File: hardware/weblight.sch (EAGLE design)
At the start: 14 parts, among them U1 ATtiny85-20SU

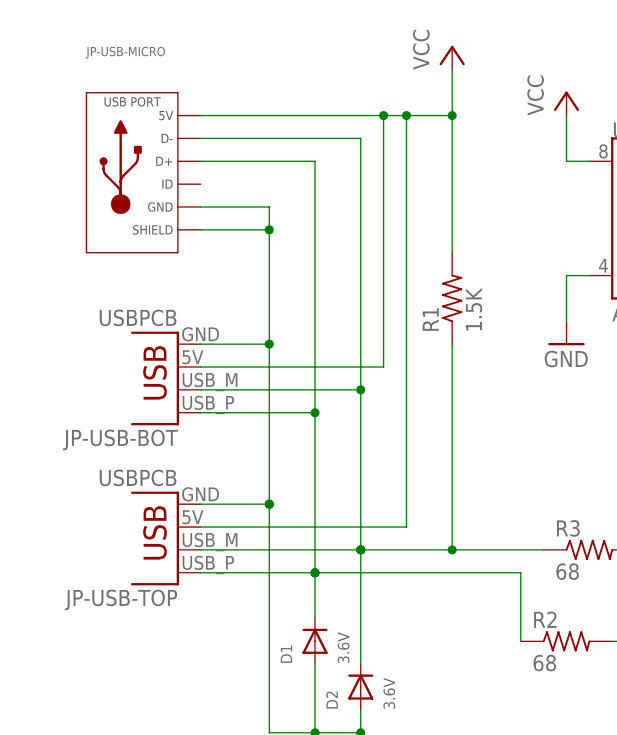
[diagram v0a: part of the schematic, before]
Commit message: #2: Remove bottom USB connector to avoid short
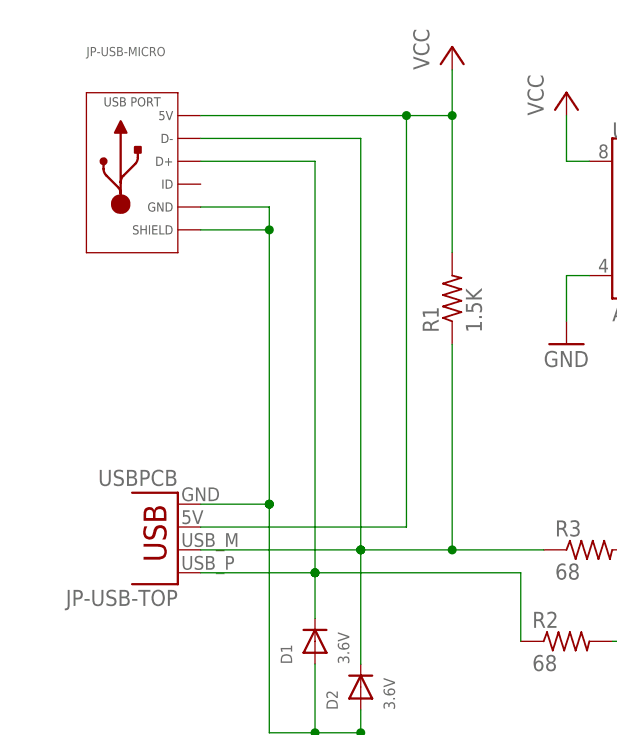
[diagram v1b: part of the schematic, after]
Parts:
- removed JP-USB-BOT: USBPCB, SparkFun-Connectors:USBPCB
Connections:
- net GND: no longer JP-USB-BOT.GND
- net USB_D_MINUS_RAW: no longer JP-USB-BOT.D-
- net USB_D_PLUS_RAW: no longer JP-USB-BOT.D+
- net VCC: no longer JP-USB-BOT.VBUS
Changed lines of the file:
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@@
 <part name="D2" library="microbuilder" deviceset="DIODE" device="SOD-523" value="3.6V"/>
 <part name="D4" library="SparkFun-LED" deviceset="WS2812B" device="" value="WS2812B"/>
-<part name="JP-USB-BOT" library="SparkFun-Connectors" deviceset="USB" device="PCB"/>
 <part name="U1" library="SparkFun-DigitalIC" deviceset="ATTINY45" device="TINY85-20-SMT" value="ATtiny85-20SU"/>
 <part name="JP-USB-MICRO" library="MF_Connectors" deviceset="USB" device="_MICRO_RIGHT"/>
@@
 <instance part="D2" gate="G$1" x="-27.94" y="22.86" rot="R90"/>
 <instance part="D4" gate="G$1" x="73.66" y="45.72"/>
-<instance part="JP-USB-BOT" gate="G$1" x="-48.26" y="60.96" rot="R180"/>
 <instance part="U1" gate="G$1" x="12.7" y="73.66"/>
 <instance part="JP-USB-MICRO" gate="G$1" x="-53.34" y="81.28"/>
@@
 <wire x1="-45.72" y1="40.64" x2="-22.86" y2="40.64" width="0.1524" layer="91"/>
 <pinref part="R1" gate="G$1" pin="2"/>
-<pinref part="JP-USB-BOT" gate="G$1" pin="VBUS"/>
-<wire x1="-45.72" y1="58.42" x2="-25.4" y2="58.42" width="0.1524" layer="91"/>
 <pinref part="JP-USB-MICRO" gate="G$1" pin="5V"/>
 <wire x1="-17.78" y1="86.36" x2="-22.86" y2="86.36" width="0.1524" layer="91"/>
 <junction x="-17.78" y="86.36"/>
 <pinref part="P+2" gate="VCC" pin="VCC"/>
-<wire x1="-22.86" y1="86.36" x2="-25.4" y2="86.36" width="0.1524" layer="91"/>
-<wire x1="-25.4" y1="86.36" x2="-45.72" y2="86.36" width="0.1524" layer="91"/>
+<wire x1="-22.86" y1="86.36" x2="-45.72" y2="86.36" width="0.1524" layer="91"/>
 <wire x1="-17.78" y1="86.36" x2="-17.78" y2="91.44" width="0.1524" layer="91"/>
 <wire x1="-17.78" y1="71.12" x2="-17.78" y2="86.36" width="0.1524" layer="91"/>
-<wire x1="-25.4" y1="58.42" x2="-25.4" y2="86.36" width="0.1524" layer="91"/>
-<junction x="-25.4" y="86.36"/>
 <wire x1="-22.86" y1="40.64" x2="-22.86" y2="86.36" width="0.1524" layer="91"/>
 <junction x="-22.86" y="86.36"/>
@@
 <pinref part="JP-USB-TOP" gate="G$1" pin="GND"/>
 <wire x1="-45.72" y1="43.18" x2="-38.1" y2="43.18" width="0.1524" layer="91"/>
-<pinref part="JP-USB-BOT" gate="G$1" pin="GND"/>
-<wire x1="-45.72" y1="60.96" x2="-38.1" y2="60.96" width="0.1524" layer="91"/>
 <pinref part="JP-USB-MICRO" gate="G$1" pin="SLD"/>
 <junction x="-38.1" y="73.66"/>
@@
 <wire x1="-45.72" y1="76.2" x2="-38.1" y2="76.2" width="0.1524" layer="91"/>
 <wire x1="-38.1" y1="76.2" x2="-38.1" y2="73.66" width="0.1524" layer="91"/>
-<wire x1="-38.1" y1="73.66" x2="-38.1" y2="60.96" width="0.1524" layer="91"/>
-<junction x="-38.1" y="60.96"/>
-<wire x1="-38.1" y1="60.96" x2="-38.1" y2="43.18" width="0.1524" layer="91"/>
+<wire x1="-38.1" y1="73.66" x2="-38.1" y2="43.18" width="0.1524" layer="91"/>
 <junction x="-38.1" y="43.18"/>
 <junction x="-38.1" y="43.18"/>
@@
 <wire x1="-27.94" y1="25.4" x2="-27.94" y2="38.1" width="0.1524" layer="91"/>
 <junction x="-27.94" y="38.1"/>
-<pinref part="JP-USB-BOT" gate="G$1" pin="D-"/>
-<wire x1="-45.72" y1="55.88" x2="-27.94" y2="55.88" width="0.1524" layer="91"/>
 <junction x="-27.94" y="38.1"/>
-<wire x1="-27.94" y1="55.88" x2="-27.94" y2="38.1" width="0.1524" layer="91"/>
-<junction x="-27.94" y="55.88"/>
-<wire x1="-27.94" y1="55.88" x2="-27.94" y2="83.82" width="0.1524" layer="91"/>
+<wire x1="-27.94" y1="38.1" x2="-27.94" y2="83.82" width="0.1524" layer="91"/>
 <pinref part="JP-USB-MICRO" gate="G$1" pin="D-"/>
 <wire x1="-27.94" y1="83.82" x2="-45.72" y2="83.82" width="0.1524" layer="91"/>
@@
 <wire x1="-33.02" y1="30.48" x2="-33.02" y2="35.56" width="0.1524" layer="91"/>
 <junction x="-33.02" y="35.56"/>
-<pinref part="JP-USB-BOT" gate="G$1" pin="D+"/>
-<wire x1="-45.72" y1="53.34" x2="-33.02" y2="53.34" width="0.1524" layer="91"/>
 <junction x="-33.02" y="35.56"/>
-<wire x1="-33.02" y1="53.34" x2="-33.02" y2="35.56" width="0.1524" layer="91"/>
-<junction x="-33.02" y="53.34"/>
 <pinref part="JP-USB-MICRO" gate="G$1" pin="D+"/>
-<wire x1="-33.02" y1="53.34" x2="-33.02" y2="81.28" width="0.1524" layer="91"/>
+<wire x1="-33.02" y1="35.56" x2="-33.02" y2="81.28" width="0.1524" layer="91"/>
 <wire x1="-33.02" y1="81.28" x2="-45.72" y2="81.28" width="0.1524" layer="91"/>
 </segment>

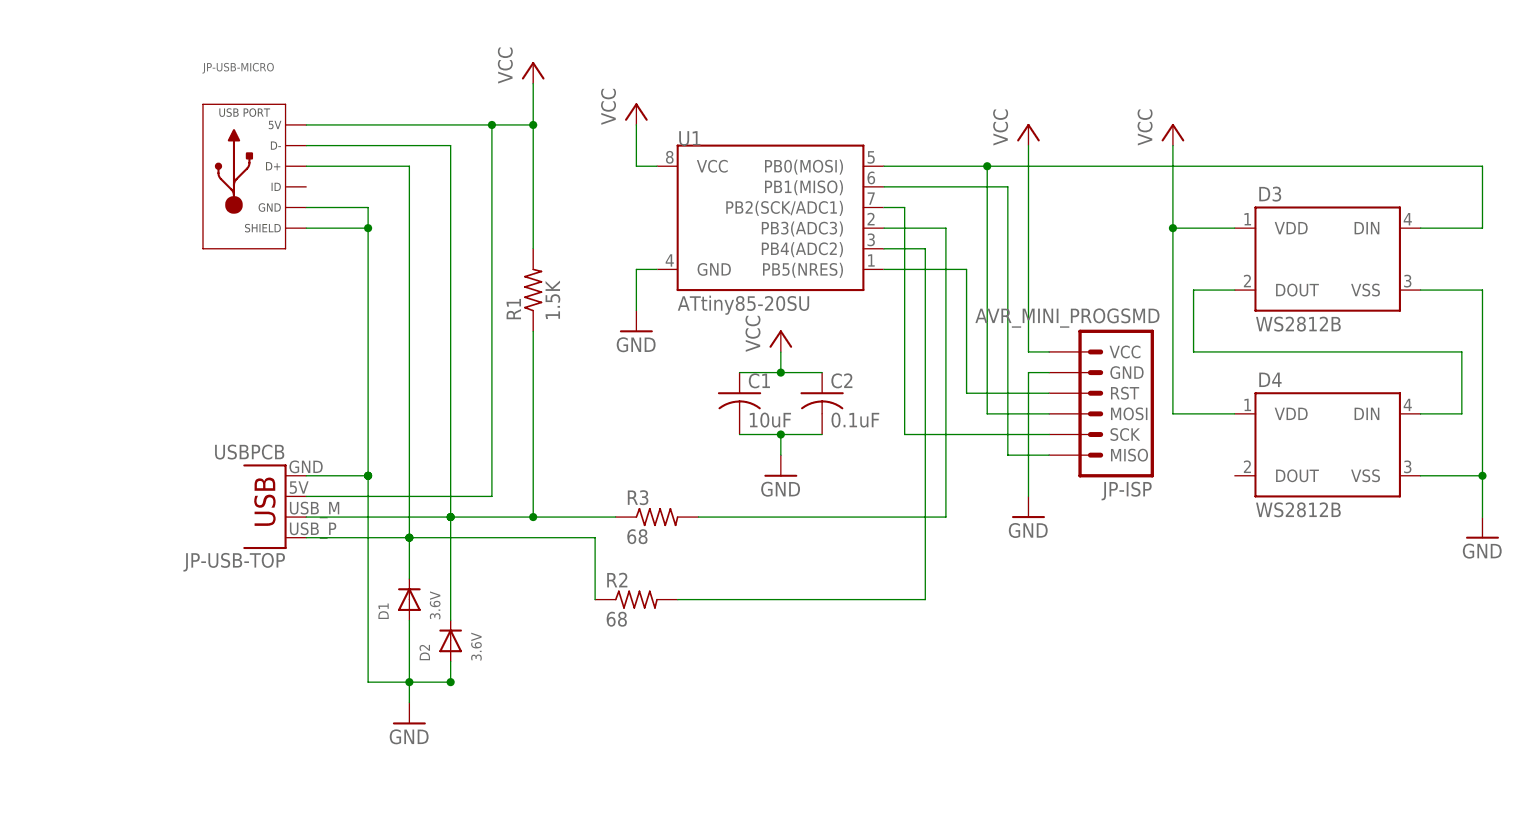
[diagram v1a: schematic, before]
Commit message: #17: add 470 ohm resistor before first DIN
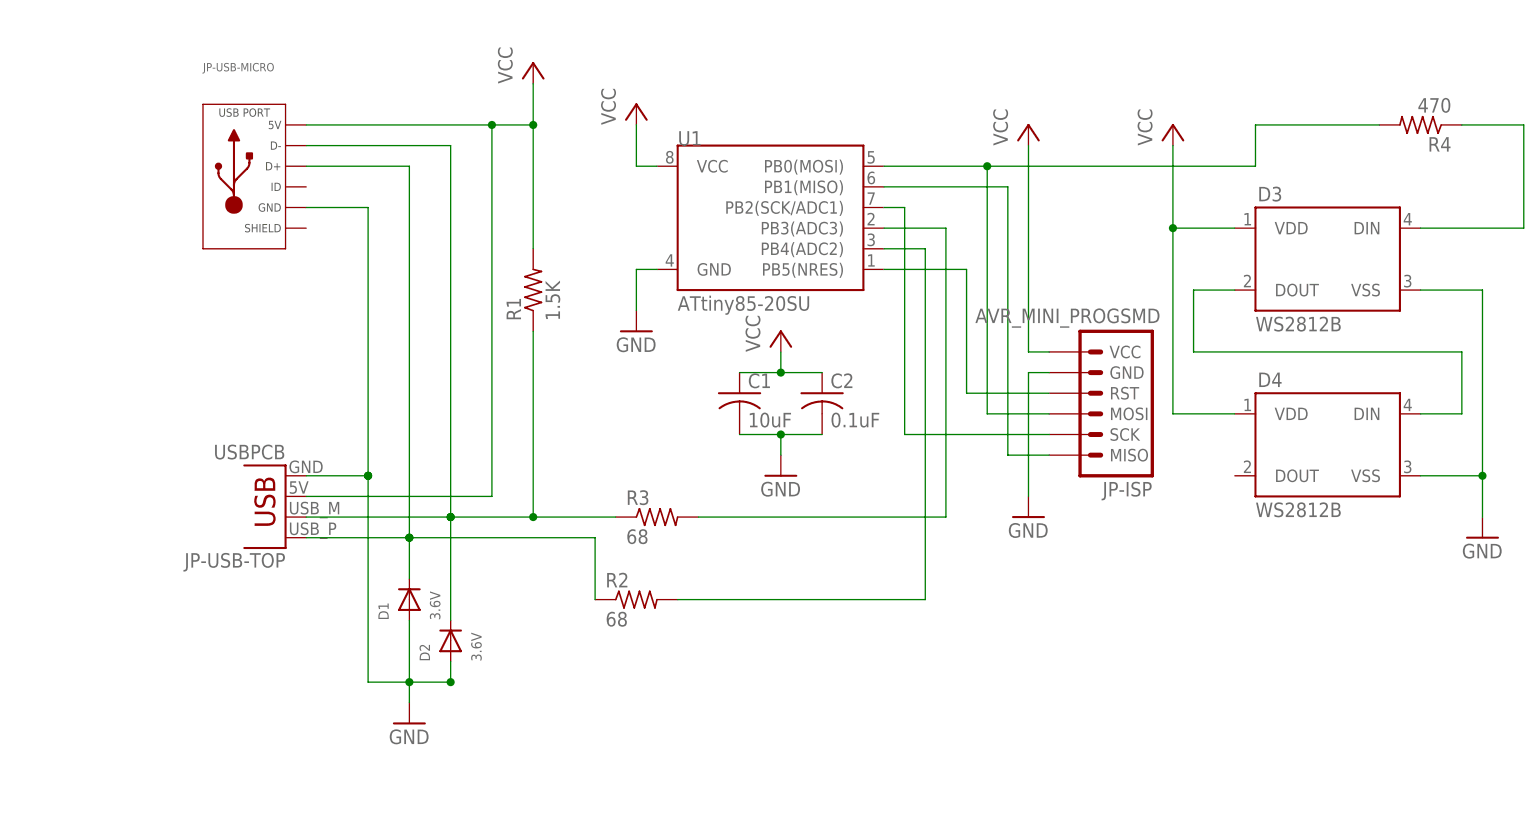
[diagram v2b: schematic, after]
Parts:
- added R4: 470, rcl:R-US_R0402
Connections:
- new net N$1: D3.DIN, R4.1
- net GND: no longer JP-USB-MICRO.SLD
- net MOSI/DIN: now also R4.2; no longer D3.DIN
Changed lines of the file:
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@@
 <grid distance="0.1" unitdist="inch" unit="inch" style="lines" multiple="1" display="no" altdistance="0.01" altunitdist="inch" altunit="inch"/>
 <layers>
-<layer number="1" name="Top" color="4" fill="1" visible="no" active="no"/>
-<layer number="16" name="Bottom" color="1" fill="1" visible="no" active="no"/>
-<layer number="17" name="Pads" color="2" fill="1" visible="no" active="no"/>
-<layer number="18" name="Vias" color="2" fill="1" visible="no" active="no"/>
-<layer number="19" name="Unrouted" color="6" fill="1" visible="no" active="no"/>
-<layer number="20" name="Dimension" color="15" fill="1" visible="no" active="no"/>
-<layer number="21" name="tPlace" color="7" fill="1" visible="no" active="no"/>
-<layer number="22" name="bPlace" color="7" fill="1" visible="no" active="no"/>
-<layer number="23" name="tOrigins" color="15" fill="1" visible="no" active="no"/>
-<layer number="24" name="bOrigins" color="15" fill="1" visible="no" active="no"/>
-<layer number="25" name="tNames" color="7" fill="1" visible="no" active="no"/>
-<layer number="26" name="bNames" color="7" fill="1" visible="no" active="no"/>
-<layer number="27" name="tValues" color="7" fill="1" visible="no" active="no"/>
-<layer number="28" name="bValues" color="7" fill="1" visible="no" active="no"/>
+<layer number="1" name="Top" color="4" fill="1" visible="yes" active="no"/>
+<layer number="16" name="Bottom" color="1" fill="1" visible="yes" active="no"/>
+<layer number="17" name="Pads" color="2" fill="1" visible="yes" active="no"/>
+<layer number="18" name="Vias" color="2" fill="1" visible="yes" active="no"/>
+<layer number="19" name="Unrouted" color="6" fill="1" visible="yes" active="no"/>
+<layer number="20" name="Dimension" color="15" fill="1" visible="yes" active="no"/>
+<layer number="21" name="tPlace" color="7" fill="1" visible="yes" active="no"/>
+<layer number="22" name="bPlace" color="7" fill="1" visible="yes" active="no"/>
+<layer number="23" name="tOrigins" color="15" fill="1" visible="yes" active="no"/>
+<layer number="24" name="bOrigins" color="15" fill="1" visible="yes" active="no"/>
+<layer number="25" name="tNames" color="7" fill="1" visible="yes" active="no"/>
+<layer number="26" name="bNames" color="7" fill="1" visible="yes" active="no"/>
+<layer number="27" name="tValues" color="7" fill="1" visible="yes" active="no"/>
+<layer number="28" name="bValues" color="7" fill="1" visible="yes" active="no"/>
 <layer number="29" name="tStop" color="7" fill="3" visible="no" active="no"/>
 <layer number="30" name="bStop" color="7" fill="6" visible="no" active="no"/>
@@
 <layer number="35" name="tGlue" color="7" fill="4" visible="no" active="no"/>
 <layer number="36" name="bGlue" color="7" fill="5" visible="no" active="no"/>
-<layer number="37" name="tTest" color="7" fill="1" visible="no" active="no"/>
-<layer number="38" name="bTest" color="7" fill="1" visible="no" active="no"/>
+<layer number="37" name="tTest" color="7" fill="1" visible="yes" active="no"/>
+<layer number="38" name="bTest" color="7" fill="1" visible="yes" active="no"/>
 <layer number="39" name="tKeepout" color="4" fill="11" visible="no" active="no"/>
 <layer number="40" name="bKeepout" color="1" fill="11" visible="no" active="no"/>
@@
 <layer number="44" name="Drills" color="7" fill="1" visible="no" active="no"/>
 <layer number="45" name="Holes" color="7" fill="1" visible="no" active="no"/>
-<layer number="46" name="Milling" color="3" fill="1" visible="no" active="no"/>
-<layer number="47" name="Measures" color="7" fill="1" visible="no" active="no"/>
-<layer number="48" name="Document" color="7" fill="1" visible="no" active="no"/>
-<layer number="49" name="Reference" color="7" fill="1" visible="no" active="no"/>
-<layer number="50" name="dxf" color="7" fill="1" visible="no" active="no"/>
-<layer number="51" name="tDocu" color="7" fill="1" visible="no" active="no"/>
-<layer number="52" name="bDocu" color="7" fill="1" visible="no" active="no"/>
-<layer number="53" name="tGND_GNDA" color="7" fill="9" visible="no" active="no"/>
-<layer number="54" name="bGND_GNDA" color="1" fill="9" visible="no" active="no"/>
-<layer number="56" name="wert" color="7" fill="1" visible="no" active="no"/>
-<layer number="57" name="tCAD" color="7" fill="1" visible="no" active="no"/>
-<layer number="59" name="tCarbon" color="7" fill="1" visible="no" active="no"/>
-<layer number="60" name="bCarbon" color="7" fill="1" visible="no" active="no"/>
+<layer number="46" name="Milling" color="3" fill="1" visible="yes" active="no"/>
+<layer number="47" name="Measures" color="7" fill="1" visible="yes" active="no"/>
+<layer number="48" name="Document" color="7" fill="1" visible="yes" active="no"/>
+<layer number="49" name="Reference" color="7" fill="1" visible="yes" active="no"/>
+<layer number="50" name="dxf" color="7" fill="1" visible="yes" active="no"/>
+<layer number="51" name="tDocu" color="7" fill="1" visible="yes" active="no"/>
+<layer number="52" name="bDocu" color="7" fill="1" visible="yes" active="no"/>
+<layer number="53" name="tGND_GNDA" color="7" fill="9" visible="yes" active="no"/>
+<layer number="54" name="bGND_GNDA" color="1" fill="9" visible="yes" active="no"/>
+<layer number="56" name="wert" color="7" fill="1" visible="yes" active="no"/>
+<layer number="57" name="tCAD" color="7" fill="1" visible="yes" active="no"/>
+<layer number="59" name="tCarbon" color="7" fill="1" visible="yes" active="no"/>
+<layer number="60" name="bCarbon" color="7" fill="1" visible="yes" active="no"/>
 <layer number="90" name="Modules" color="5" fill="1" visible="yes" active="yes"/>
 <layer number="91" name="Nets" color="2" fill="1" visible="yes" active="yes"/>
@@
 <part name="GND4" library="supply1" deviceset="GND" device=""/>
 <part name="P+5" library="supply1" deviceset="VCC" device=""/>
+<part name="R4" library="rcl" deviceset="R-US_" device="R0402" value="470"/>
 </parts>
 <sheets>
@@
 <instance part="GND4" gate="1" x="99.06" y="35.56"/>
 <instance part="P+5" gate="VCC" x="60.96" y="86.36"/>
+<instance part="R4" gate="G$1" x="91.44" y="86.36" rot="R180"/>
 </instances>
 <busses>
@@
 <pinref part="JP-USB-TOP" gate="G$1" pin="GND"/>
 <wire x1="-45.72" y1="43.18" x2="-38.1" y2="43.18" width="0.1524" layer="91"/>
-<pinref part="JP-USB-MICRO" gate="G$1" pin="SLD"/>
-<junction x="-38.1" y="73.66"/>
-<wire x1="-38.1" y1="73.66" x2="-45.72" y2="73.66" width="0.1524" layer="91"/>
 <pinref part="JP-USB-MICRO" gate="G$1" pin="GND"/>
 <wire x1="-45.72" y1="76.2" x2="-38.1" y2="76.2" width="0.1524" layer="91"/>
-<wire x1="-38.1" y1="76.2" x2="-38.1" y2="73.66" width="0.1524" layer="91"/>
-<wire x1="-38.1" y1="73.66" x2="-38.1" y2="43.18" width="0.1524" layer="91"/>
+<wire x1="-38.1" y1="76.2" x2="-38.1" y2="43.18" width="0.1524" layer="91"/>
 <junction x="-38.1" y="43.18"/>
 <junction x="-38.1" y="43.18"/>
@@
 <net name="MOSI/DIN" class="0">
 <segment>
-<pinref part="D3" gate="G$1" pin="DIN"/>
-<wire x1="99.06" y1="73.66" x2="91.44" y2="73.66" width="0.1524" layer="91"/>
-<wire x1="38.1" y1="81.28" x2="99.06" y2="81.28" width="0.1524" layer="91"/>
-<wire x1="99.06" y1="81.28" x2="99.06" y2="73.66" width="0.1524" layer="91"/>
+<wire x1="38.1" y1="81.28" x2="71.12" y2="81.28" width="0.1524" layer="91"/>
 <junction x="38.1" y="81.28"/>
 <pinref part="U1" gate="G$1" pin="PB0(MOSI)"/>
@@
 <wire x1="38.1" y1="81.28" x2="38.1" y2="50.8" width="0.1524" layer="91"/>
 <wire x1="38.1" y1="50.8" x2="45.72" y2="50.8" width="0.1524" layer="91"/>
+<wire x1="71.12" y1="81.28" x2="71.12" y2="86.36" width="0.1524" layer="91"/>
+<pinref part="R4" gate="G$1" pin="2"/>
+<wire x1="71.12" y1="86.36" x2="86.36" y2="86.36" width="0.1524" layer="91"/>
 </segment>
 </net>
@@
 </segment>
 </net>
+<net name="N$1" class="0">
+<segment>
+<pinref part="D3" gate="G$1" pin="DIN"/>
+<wire x1="104.14" y1="73.66" x2="91.44" y2="73.66" width="0.1524" layer="91"/>
+<wire x1="104.14" y1="73.66" x2="104.14" y2="86.36" width="0.1524" layer="91"/>
+<pinref part="R4" gate="G$1" pin="1"/>
+<wire x1="104.14" y1="86.36" x2="96.52" y2="86.36" width="0.1524" layer="91"/>
+</segment>
+</net>

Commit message: Changes to prod circuit.
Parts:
- removed JP-ISP: AVR_MINI_PROGSMD, SparkFun-Connectors:AVR_MINI_PROGSMD
- added D5, D6: WS2812B, SparkFun-LED:WS2812B
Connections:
- removed net MISO: JP-ISP.MISO, U1.PB1(MISO)
- removed net RESET: JP-ISP.RST, U1.PB5(NRES)
- removed net SCK: JP-ISP.SCK, U1.PB2(SCK/ADC1)
- new net N$2: D5.DOUT, D6.DIN
- new net N$3: D4.DOUT, D5.DIN
- net GND: now also D5.VSS, D6.VSS; no longer JP-ISP.GND
- net MOSI/DIN: no longer JP-ISP.MOSI
- net USB_D_MINUS: now also R3.1; no longer R3.2
- net USB_D_MINUS_RAW: now also R3.2; no longer R3.1
- net VCC: now also D5.VDD, D6.VDD; no longer JP-ISP.VCC
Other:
- moved on the sheet: D3, D4, R4

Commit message: Fix net names.
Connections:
- net MOSI/DIN renamed DIN_RAW
- net N$1 renamed DIN_1
- net N$2 renamed DIN_4
- net N$3 renamed DIN_3
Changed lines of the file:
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@@
 </segment>
 </net>
-<net name="MOSI/DIN" class="0">
+<net name="DIN_RAW" class="0">
 <segment>
 <wire x1="25.4" y1="81.28" x2="30.48" y2="81.28" width="0.1524" layer="91"/>
@@
 </segment>
 </net>
-<net name="N$1" class="0">
+<net name="DIN_1" class="0">
 <segment>
 <pinref part="D3" gate="G$1" pin="DIN"/>
@@
 </segment>
 </net>
-<net name="N$3" class="0">
+<net name="DIN_3" class="0">
 <segment>
 <pinref part="D4" gate="G$1" pin="DOUT"/>
@@
 </segment>
 </net>
-<net name="N$2" class="0">
+<net name="DIN_4" class="0">
 <segment>
 <pinref part="D5" gate="G$1" pin="DOUT"/>
